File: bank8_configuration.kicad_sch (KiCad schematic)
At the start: 19 parts, among them U1 ECP5-BGA256, U10 W25Q32JVSS

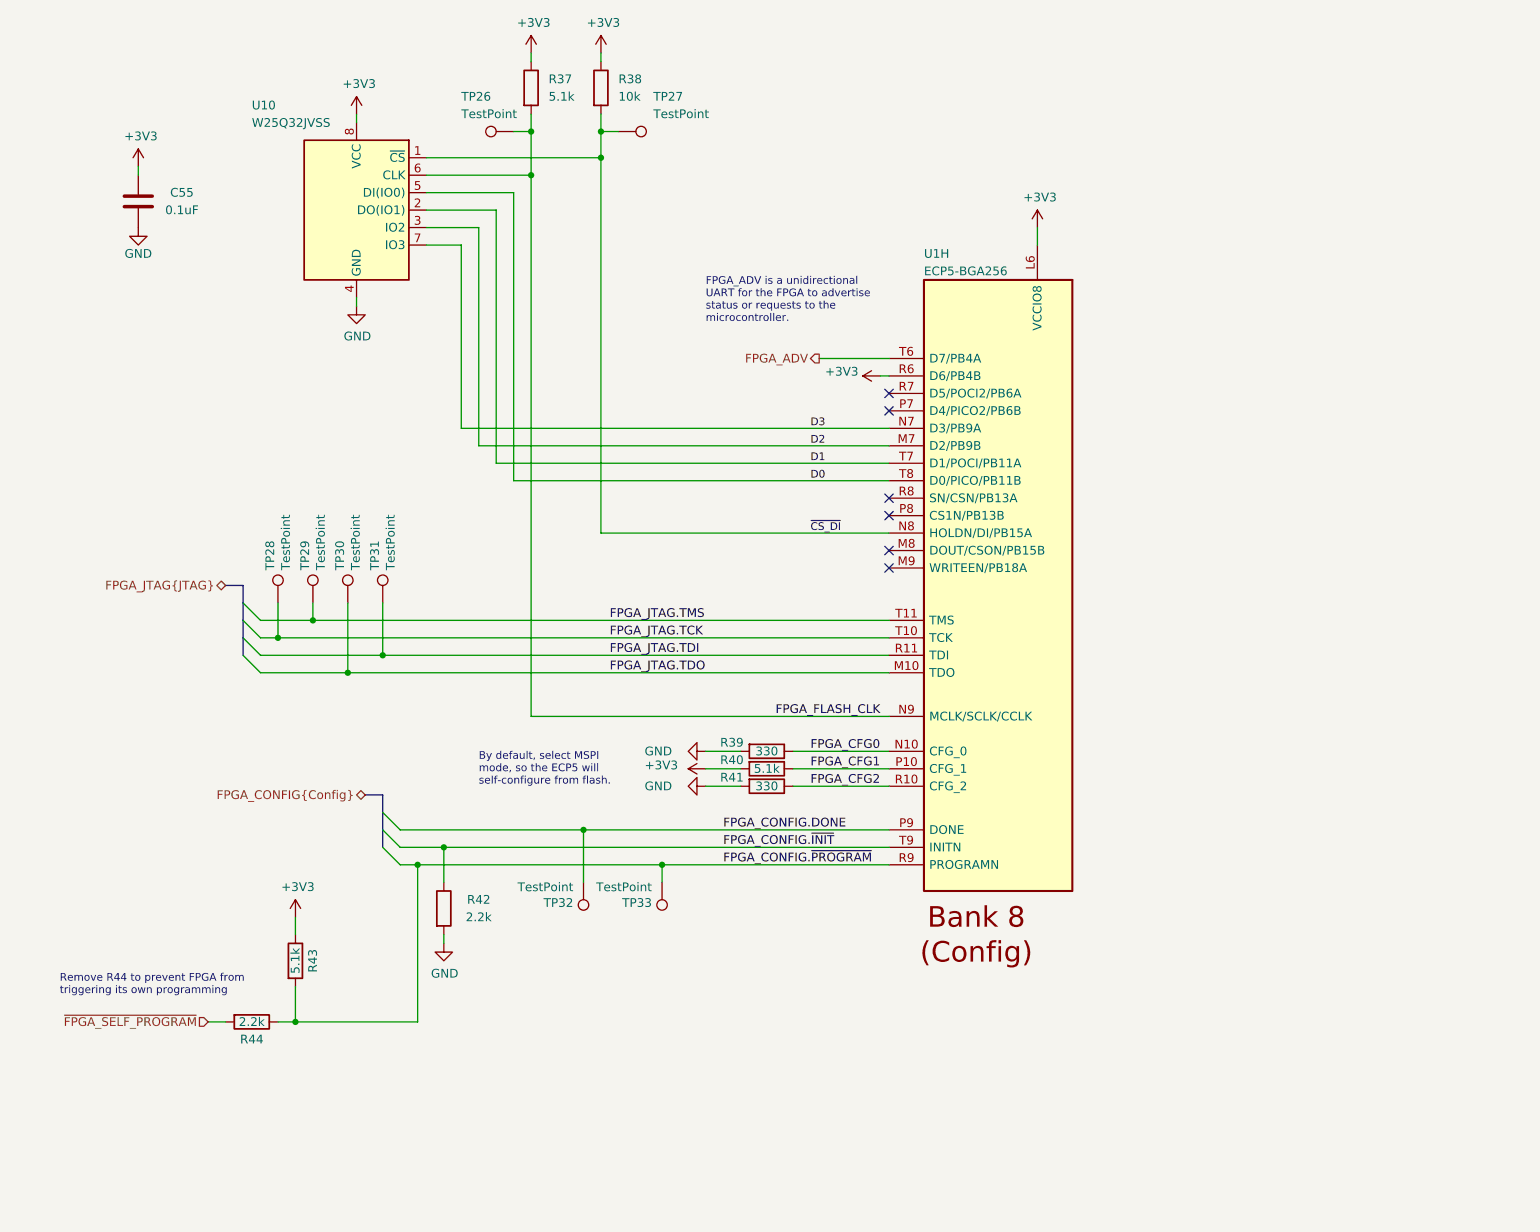
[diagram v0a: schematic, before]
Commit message: Add radio transceiver
Remove Cynthion-specific features
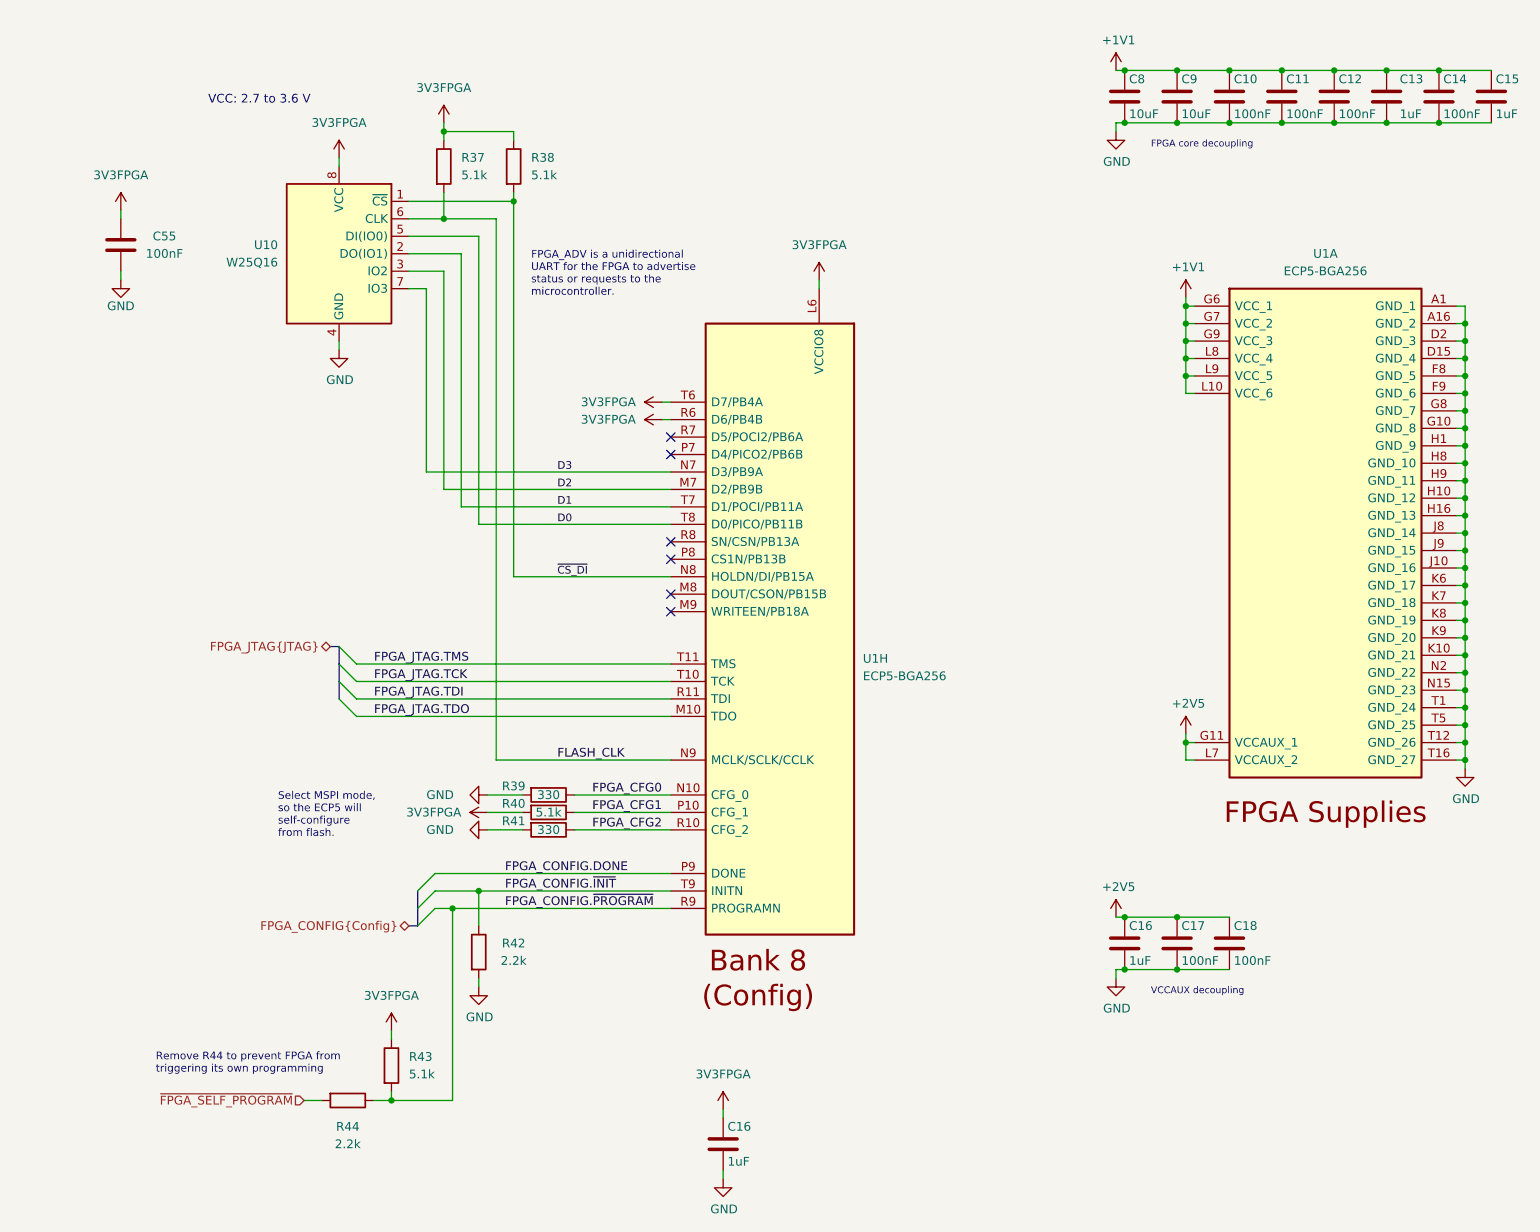
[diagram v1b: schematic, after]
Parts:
- removed TP26, TP27, TP28, TP29, TP30, TP31, TP32, TP33: TestPoint, TestPoint:TestPoint_Pad_D1.0mm, symbol Connector:TestPoint
- added C10, C11, C12, C14, C17, C18: 100nF, Capacitor_SMD:C_0402_1005Metric, symbol Device:C
- added C13, C15, C16 (x2): 1uF, Capacitor_SMD:C_0402_1005Metric, symbol Device:C
- added C8, C9: 10uF, Capacitor_SMD:C_0603_1608Metric, symbol Device:C
- added unit 1 of U1
- C55: value 0.1uF -> 100nF
- R38: value 10k -> 5.1k; Part Number RC0402JR-0710KL -> RC0402JR-075K1L
- U10: value W25Q32JVSS -> W25Q16; Part Number W25Q32JVSSIQ -> W25Q16JVSSIQ
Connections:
- net FPGA_ADV is gone; now on net 3V3FPGA: U1.T6 (D7/PB4A)
- net GND: now also C10.2, C11.2, C12.2, C13.2, C14.2, C15.2, C16.2, C16.2, C17.2, C18.2, C8.2, C9.2, U1.A1 (GND_1), U1.A16 (GND_2), U1.D15 (GND_4), U1.D2 (GND_3), U1.F8 (GND_5), U1.F9 (GND_6), U1.G10 (GND_8), U1.G8 (GND_7), U1.H1 (GND_9), U1.H10 (GND_12), U1.H16 (GND_13), U1.H8 (GND_10), U1.H9 (GND_11), U1.J10 (GND_16), U1.J8 (GND_14), U1.J9 (GND_15), U1.K10 (GND_21), U1.K6 (GND_17), U1.K7 (GND_18), U1.K8 (GND_19), U1.K9 (GND_20), U1.N15 (GND_23), U1.N2 (GND_22), U1.T1 (GND_24), U1.T12 (GND_26), U1.T16 (GND_27), U1.T5 (GND_25)
- net +3V3 renamed 3V3FPGA
- net 3V3FPGA: now also C16.1
- net FPGA_FLASH_CLK renamed FLASH_CLK
- new net +1V1: C10.1, C11.1, C12.1, C13.1, C14.1, C15.1, C8.1, C9.1, U1.G6 (VCC_1), U1.G7 (VCC_2), U1.G9 (VCC_3), U1.L10 (VCC_6), U1.L8 (VCC_4), U1.L9 (VCC_5)
- new net +2V5: C16.1, C17.1, C18.1, U1.G11 (VCCAUX_1), U1.L7 (VCCAUX_2)
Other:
- note added: "FPGA core decoupling"
- note added: "Select MSPI mode, so the ECP5 will self-configure from flash."
- note added: "VCC: 2.7 to 3.6 V"
- note added: "VCCAUX decoupling"
- note removed: "By default, select MSPI mode, so the ECP5 will self-configure from flash."
- company: Copyright 2023 Great Scott Gadgets -> ${COPYRIGHT}
- title: URTI Mainboard -> ${TITLE}
- moved on the sheet: C55, R37, R39, R40, R41, R42, R43, R44, U10, U1H

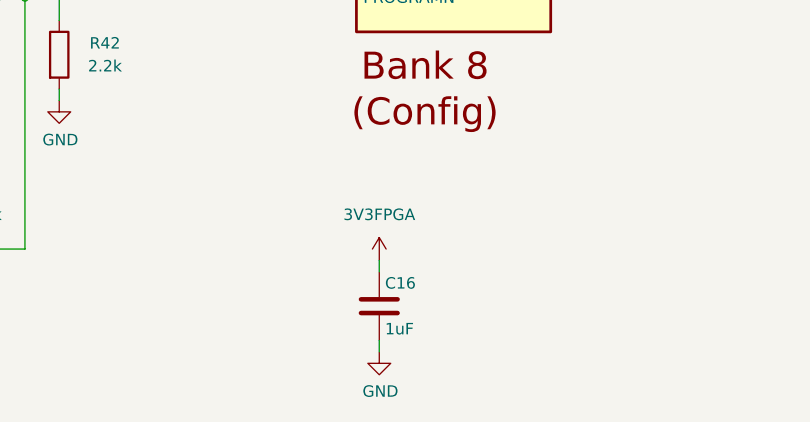
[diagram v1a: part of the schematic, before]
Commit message: Replace open drain clock inverters with push-pull
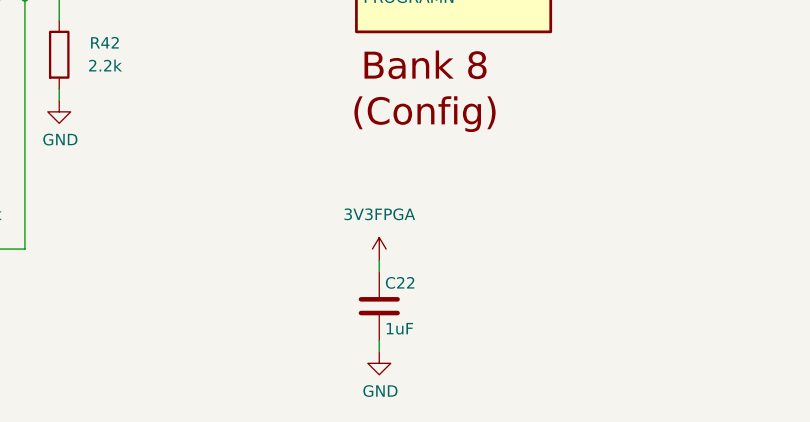
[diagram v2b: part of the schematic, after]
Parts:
- renumbered C16 to C22
